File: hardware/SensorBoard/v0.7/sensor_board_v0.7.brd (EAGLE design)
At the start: 52.5 x 43 mm, 48 parts, among them J3 USB-MICROB, U1 ATMEGA328P, U10 CCS811, U11 RFM69HW, U2 TSL2561, U4 MPL115A, U5 FT231XS, U7 SHT31, U8 MCP1703/3.3V, U9 MCP1703CB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

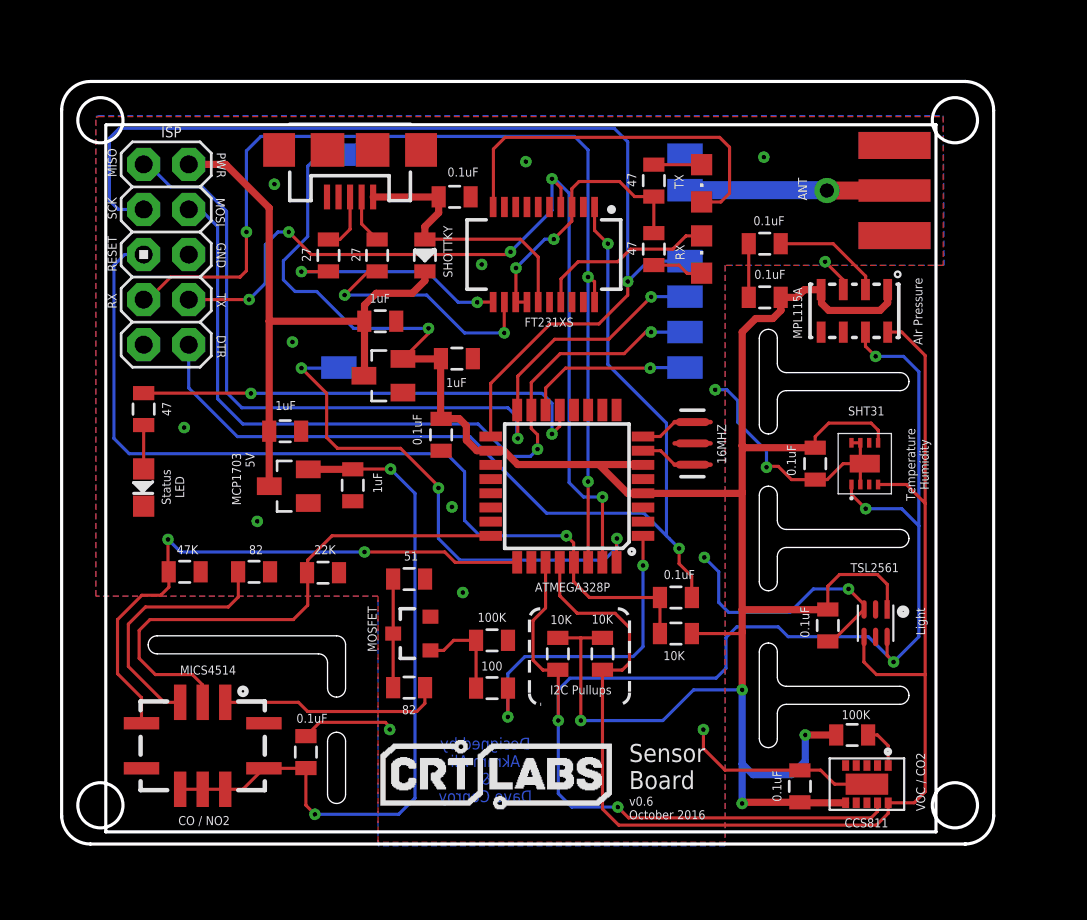
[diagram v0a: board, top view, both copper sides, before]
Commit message: v0.7 - design changes
- Adjusted I2C traces
- Increased thermal isolation to fit new board dimensions
- Moved SMA antenna pads to the top
- Adjusted MiCS 4514 sensor position
- Silkscreen adjustments
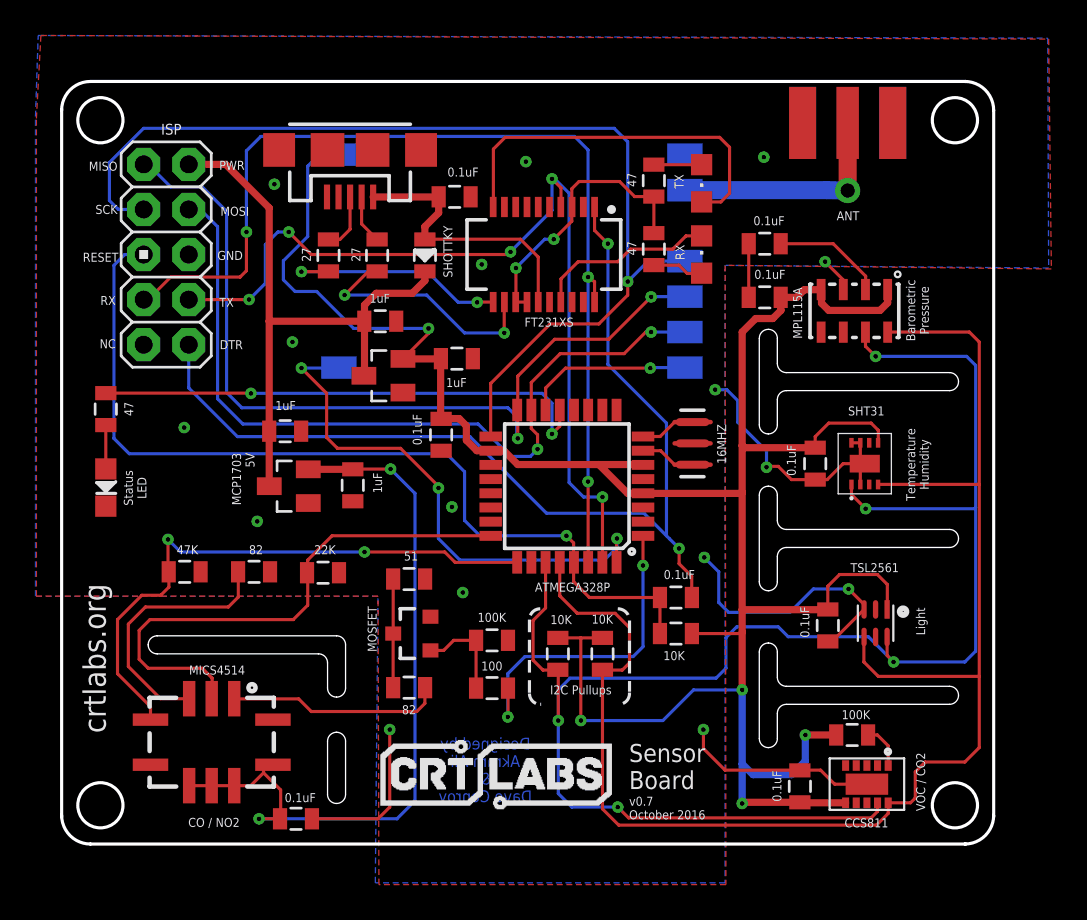
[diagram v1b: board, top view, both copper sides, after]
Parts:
- moved X1 7.48 mm to (47.7, 48.6), turned to 270 degrees
- moved C7 3.80 mm to (16.6, 7.37), turned to 0 degrees
- moved LED2 2.13 mm to (5.89, 26.0)
- moved R4 2.13 mm to (5.89, 30.5)
- moved MICS4514 0.55 mm to (11.9, 11.7)
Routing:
- net SCL: track 73.3 -> 84.9 mm
- net SDA: track 85.5 -> 95.5 mm
- net GND: track 52.0 -> 55.7 mm
- net 5V: track 40.2 -> 42.6 mm
- net N$2: track 26.5 -> 28.6 mm
- net ANT: track 11.8 -> 13.0 mm
- net SCK: track 60.5 -> 59.7 mm
- net VNOX: track 30.3 -> 30.9 mm
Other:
- outline, holes or cut-outs redrawn
- board text added: "Barometric Pressure"
- board text added: "NC"
- board text added: "v0.7 October 2016"
- board text removed: "AIr Pressure"
- board text removed: "v0.6 October 2016"

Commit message: Adjusted microUSB port towards the edge
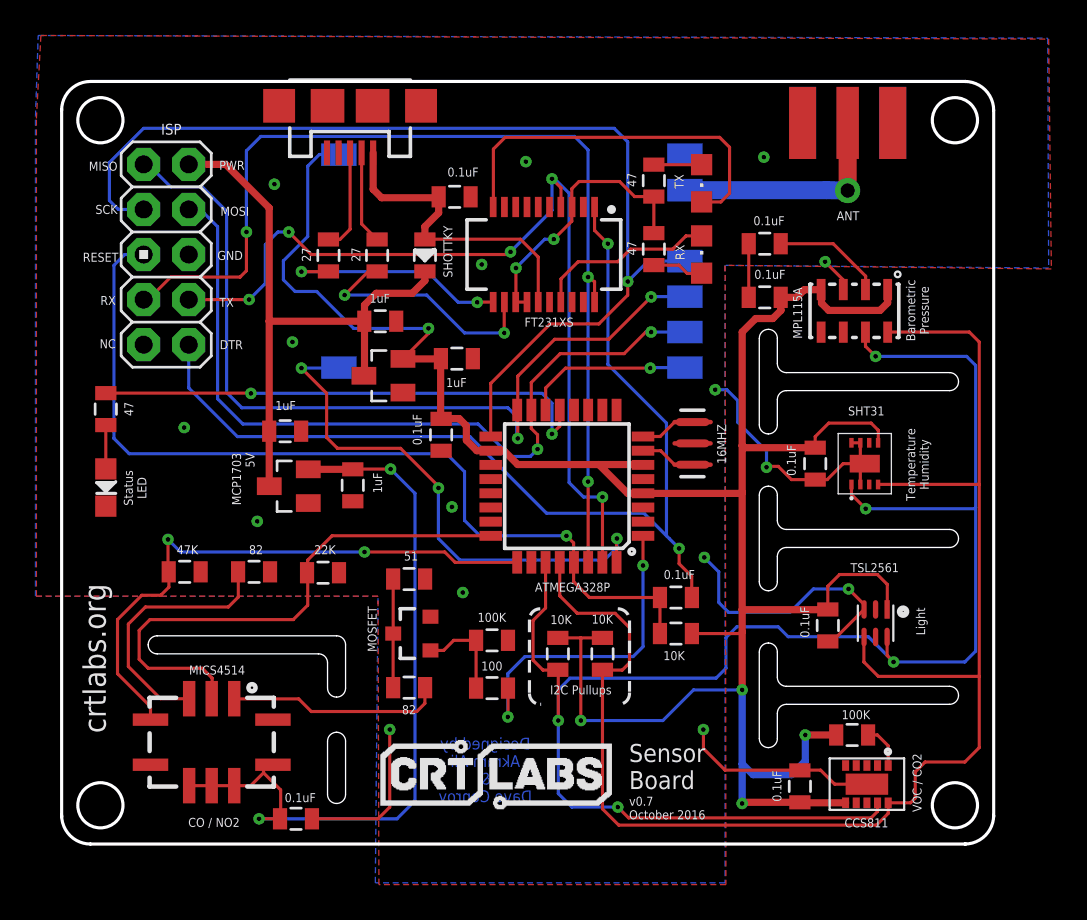
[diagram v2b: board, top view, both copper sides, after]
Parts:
- moved J3 2.49 mm to (19.7, 47.5)
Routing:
- net N$33: track 3.28 -> 5.77 mm
- net N$32: track 2.76 -> 5.24 mm
- net VBUS: track 15.8 -> 18.1 mm
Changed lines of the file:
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@@
 Humidity</text>
 <text x="52.07" y="18.4912" size="0.508" layer="121" font="vector" rot="R90" align="bottom-center">Light</text>
-<text x="52.07" y="9.4488" size="0.508" layer="121" font="vector" rot="R90" align="bottom-center">VOC / CO2</text>
+<text x="51.8668" y="9.398" size="0.508" layer="121" font="vector" rot="R90" align="bottom-center">VOC / CO2</text>
 <text x="52.2732" y="36.0172" size="0.508" layer="121" font="vector" rot="R90" align="bottom-center">Barometric
 Pressure</text>
@@
 <attribute name="VALUE" x="20.955" y="26.8732" size="0.508" layer="121" font="vector" rot="R270"/>
 </element>
-<element name="J3" library="SparkFun-Connectors" package="USB-MICROB" value="USB-MICROB" x="19.6596" y="45.0596" smashed="yes" rot="R180">
-<attribute name="PROD_ID" value="CONN-09505" x="19.6596" y="45.0596" size="1.778" layer="27" rot="R180" display="off"/>
+<element name="J3" library="SparkFun-Connectors" package="USB-MICROB" value="USB-MICROB" x="19.6596" y="47.5488" smashed="yes" rot="R180">
+<attribute name="PROD_ID" value="CONN-09505" x="19.6596" y="47.5488" size="1.778" layer="27" rot="R180" display="off"/>
 </element>
 <element name="U5" library="SparkFun-DigitalIC" package="SSOP20_L" value="FT231XS" x="30.5816" y="39.1668" smashed="yes" rot="R180">
@@
 <wire x1="29.2608" y1="40.0304" x2="23.8904" y2="40.0304" width="0.1778" layer="1"/>
 <wire x1="23.8904" y1="40.0304" x2="23.876" y2="40.016" width="0.1778" layer="1"/>
-<wire x1="20.9596" y1="42.4096" x2="24.644" y2="42.4096" width="0.4064" layer="1"/>
 <wire x1="24.644" y1="42.4096" x2="24.6524" y2="42.418" width="0.4064" layer="1"/>
 <wire x1="24.6524" y1="42.418" x2="24.6524" y2="41.518" width="0.4064" layer="1"/>
 <wire x1="24.6524" y1="41.518" x2="23.876" y2="40.7416" width="0.4064" layer="1"/>
 <wire x1="23.876" y1="40.7416" x2="23.876" y2="40.016" width="0.4064" layer="1"/>
+<wire x1="20.9596" y1="44.8988" x2="20.9596" y2="42.8452" width="0.4064" layer="1"/>
+<wire x1="20.9596" y1="42.8452" x2="21.4376" y2="42.3672" width="0.4064" layer="1"/>
+<wire x1="21.4376" y1="42.3672" x2="24.6016" y2="42.3672" width="0.4064" layer="1"/>
+<wire x1="24.6016" y1="42.3672" x2="24.6524" y2="42.418" width="0.4064" layer="1"/>
 </signal>
 <signal name="N$32">
 <contactref element="R21" pad="2"/>
 <contactref element="J3" pad="D-"/>
-<wire x1="20.3096" y1="42.4096" x2="20.3096" y2="40.89" width="0.1778" layer="1"/>
+<wire x1="20.3096" y1="44.8988" x2="20.3096" y2="40.89" width="0.1778" layer="1"/>
 <wire x1="20.3096" y1="40.89" x2="21.1836" y2="40.016" width="0.1778" layer="1"/>
 </signal>
@@
 <wire x1="18.4404" y1="40.016" x2="19.0864" y2="40.016" width="0.1778" layer="1"/>
 <wire x1="19.0864" y1="40.016" x2="19.6596" y2="40.5892" width="0.1778" layer="1"/>
-<wire x1="19.6596" y1="40.5892" x2="19.6596" y2="42.4096" width="0.1778" layer="1"/>
+<wire x1="19.6596" y1="40.5892" x2="19.6596" y2="44.8988" width="0.1778" layer="1"/>
 </signal>
 <signal name="FTDI_VCC">

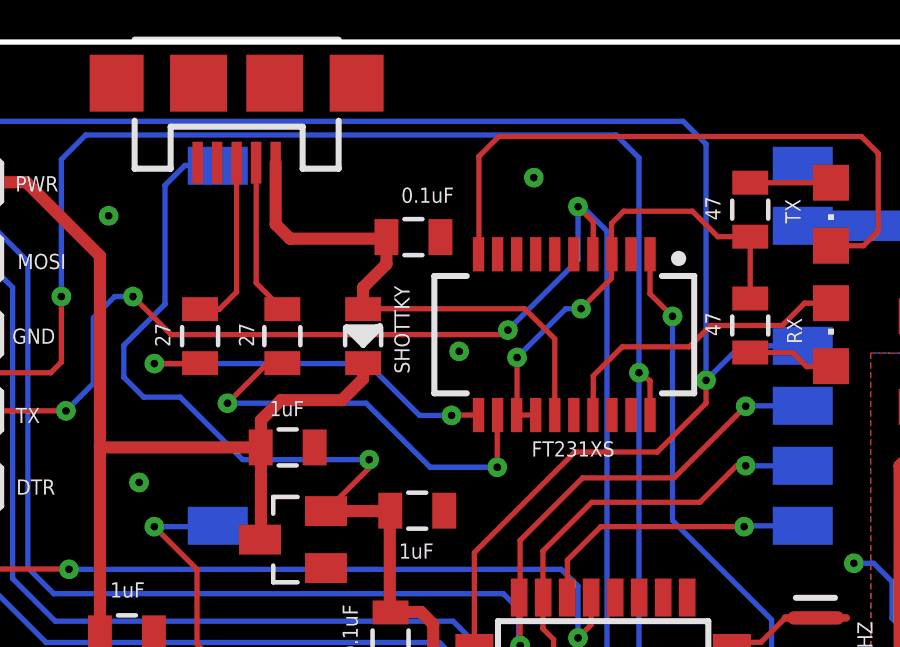
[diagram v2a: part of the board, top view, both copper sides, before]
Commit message: cap trace adjustment
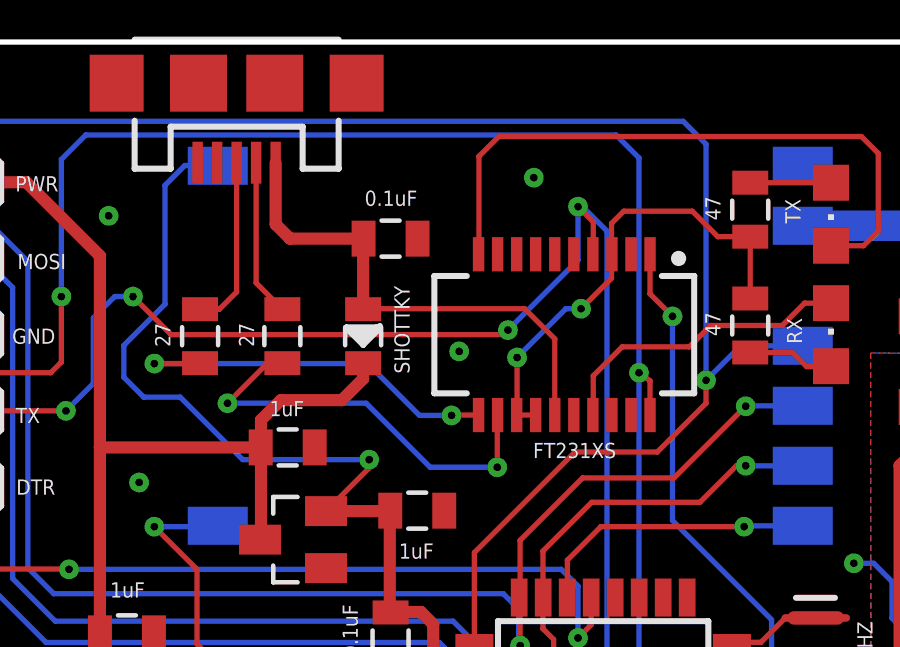
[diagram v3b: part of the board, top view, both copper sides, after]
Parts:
- moved C11 0.76 mm to (24.8, 42.4)
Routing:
- net VBUS: track 18.1 -> 16.9 mm
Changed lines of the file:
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@@
 <element name="U5" library="SparkFun-DigitalIC" package="SSOP20_L" value="FT231XS" x="30.5816" y="39.1668" smashed="yes" rot="R180">
 <attribute name="PROD_ID" value="IC-11524" x="30.5816" y="39.1668" size="1.778" layer="27" rot="R180" display="off"/>
-<attribute name="VALUE" x="32.258" y="35.6108" size="0.508" layer="121" font="vector" rot="R180"/>
+<attribute name="VALUE" x="32.3088" y="35.56" size="0.508" layer="121" font="vector" rot="R180"/>
 </element>
 <element name="RX" library="adafruit" package="CHIPLED_0805" value="Green" x="39.4716" y="39.1668" smashed="yes">
@@
 <attribute name="VALUE" x="20.2438" y="38.7604" size="0.508" layer="121" font="vector" rot="R90"/>
 </element>
-<element name="C11" library="SparkFun-Capacitors" package="0805" value="0.1uF" x="25.5524" y="42.418" smashed="yes">
-<attribute name="MF" value="" x="25.5524" y="42.418" size="1.778" layer="27" display="off"/>
-<attribute name="MPN" value="" x="25.5524" y="42.418" size="1.778" layer="27" display="off"/>
-<attribute name="OC_NEWARK" value="unknown" x="25.5524" y="42.418" size="1.778" layer="27" display="off"/>
-<attribute name="VALUE" x="25.146" y="43.561" size="0.508" layer="121" font="vector"/>
+<element name="C11" library="SparkFun-Capacitors" package="0805" value="0.1uF" x="24.7904" y="42.3672" smashed="yes">
+<attribute name="MF" value="" x="24.7904" y="42.3672" size="1.778" layer="27" display="off"/>
+<attribute name="MPN" value="" x="24.7904" y="42.3672" size="1.778" layer="27" display="off"/>
+<attribute name="OC_NEWARK" value="unknown" x="24.7904" y="42.3672" size="1.778" layer="27" display="off"/>
+<attribute name="VALUE" x="23.9268" y="43.4594" size="0.508" layer="121" font="vector"/>
 </element>
 <element name="U11" library="RFM69 USB Gateway" package="LOWPOWERLAB_RFM69W-MINPADS" value="RFM69HW" x="30.5308" y="37.7952" smashed="yes" rot="MR180">
@@
 <wire x1="29.2608" y1="40.0304" x2="23.8904" y2="40.0304" width="0.1778" layer="1"/>
 <wire x1="23.8904" y1="40.0304" x2="23.876" y2="40.016" width="0.1778" layer="1"/>
-<wire x1="24.644" y1="42.4096" x2="24.6524" y2="42.418" width="0.4064" layer="1"/>
-<wire x1="24.6524" y1="42.418" x2="24.6524" y2="41.518" width="0.4064" layer="1"/>
-<wire x1="24.6524" y1="41.518" x2="23.876" y2="40.7416" width="0.4064" layer="1"/>
-<wire x1="23.876" y1="40.7416" x2="23.876" y2="40.016" width="0.4064" layer="1"/>
 <wire x1="20.9596" y1="44.8988" x2="20.9596" y2="42.8452" width="0.4064" layer="1"/>
 <wire x1="20.9596" y1="42.8452" x2="21.4376" y2="42.3672" width="0.4064" layer="1"/>
-<wire x1="21.4376" y1="42.3672" x2="24.6016" y2="42.3672" width="0.4064" layer="1"/>
-<wire x1="24.6016" y1="42.3672" x2="24.6524" y2="42.418" width="0.4064" layer="1"/>
+<wire x1="21.4376" y1="42.3672" x2="23.8904" y2="42.3672" width="0.4064" layer="1"/>
+<wire x1="23.876" y1="40.016" x2="23.876" y2="42.3528" width="0.4064" layer="1"/>
+<wire x1="23.876" y1="42.3528" x2="23.8904" y2="42.3672" width="0.4064" layer="1"/>
 </signal>
 <signal name="N$32">
